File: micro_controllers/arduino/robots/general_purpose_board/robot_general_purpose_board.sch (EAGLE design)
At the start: 46 parts, among them IC1 ATMEGA328, IC2 7805, IC3 L293D, IC4 358, IC5 358, Q1 16MHZ

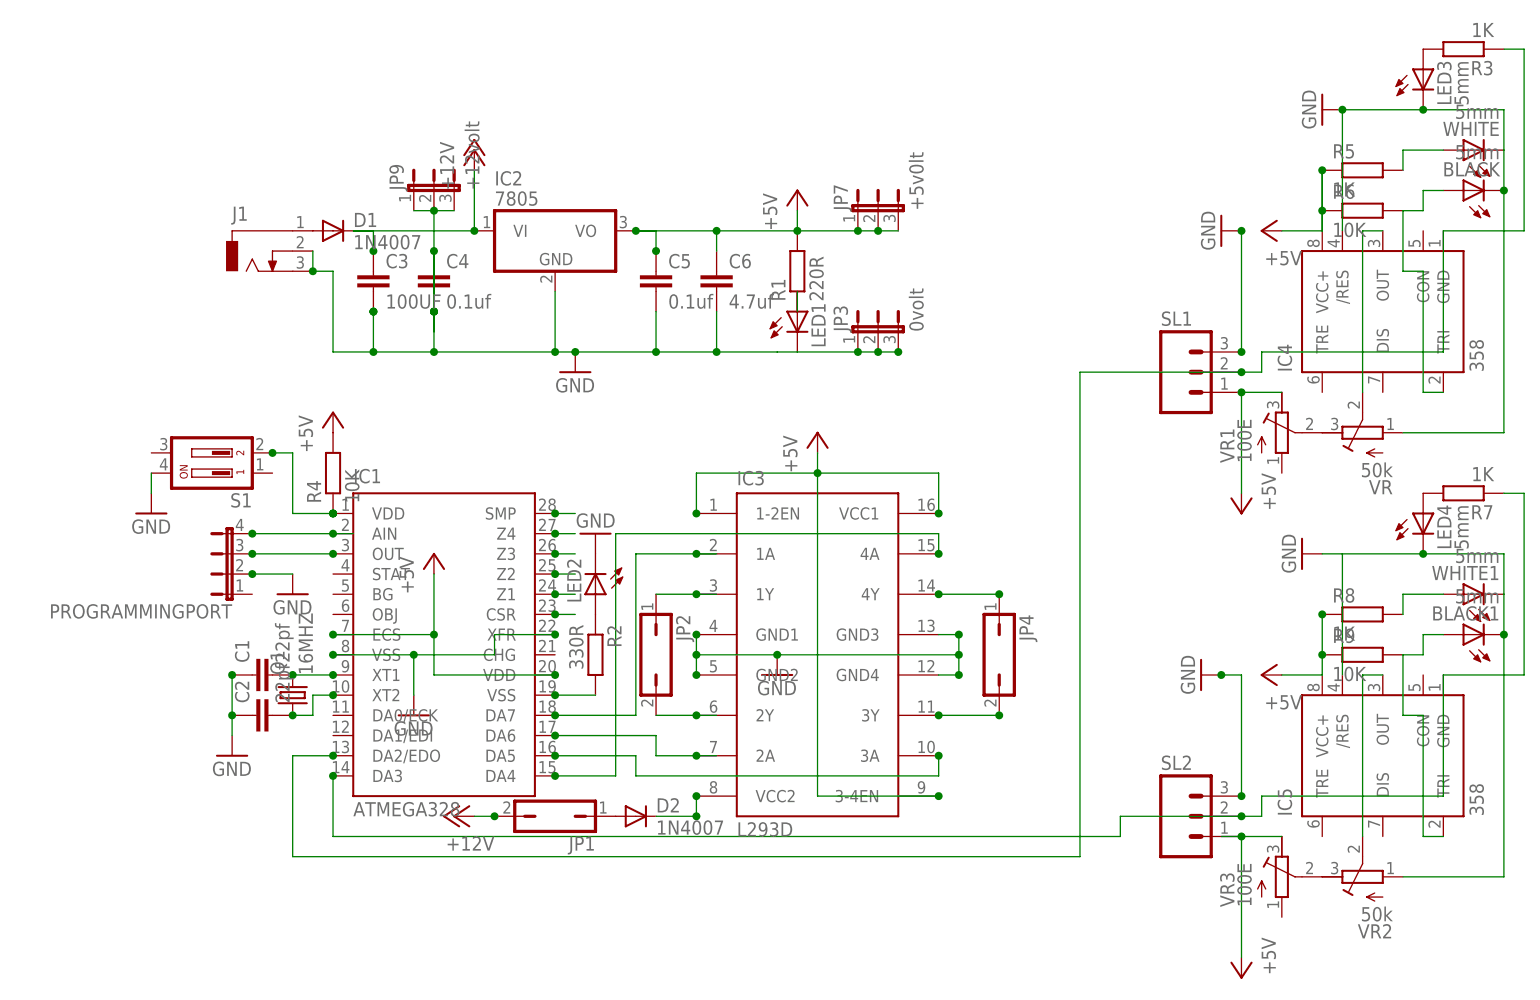
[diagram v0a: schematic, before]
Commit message: 
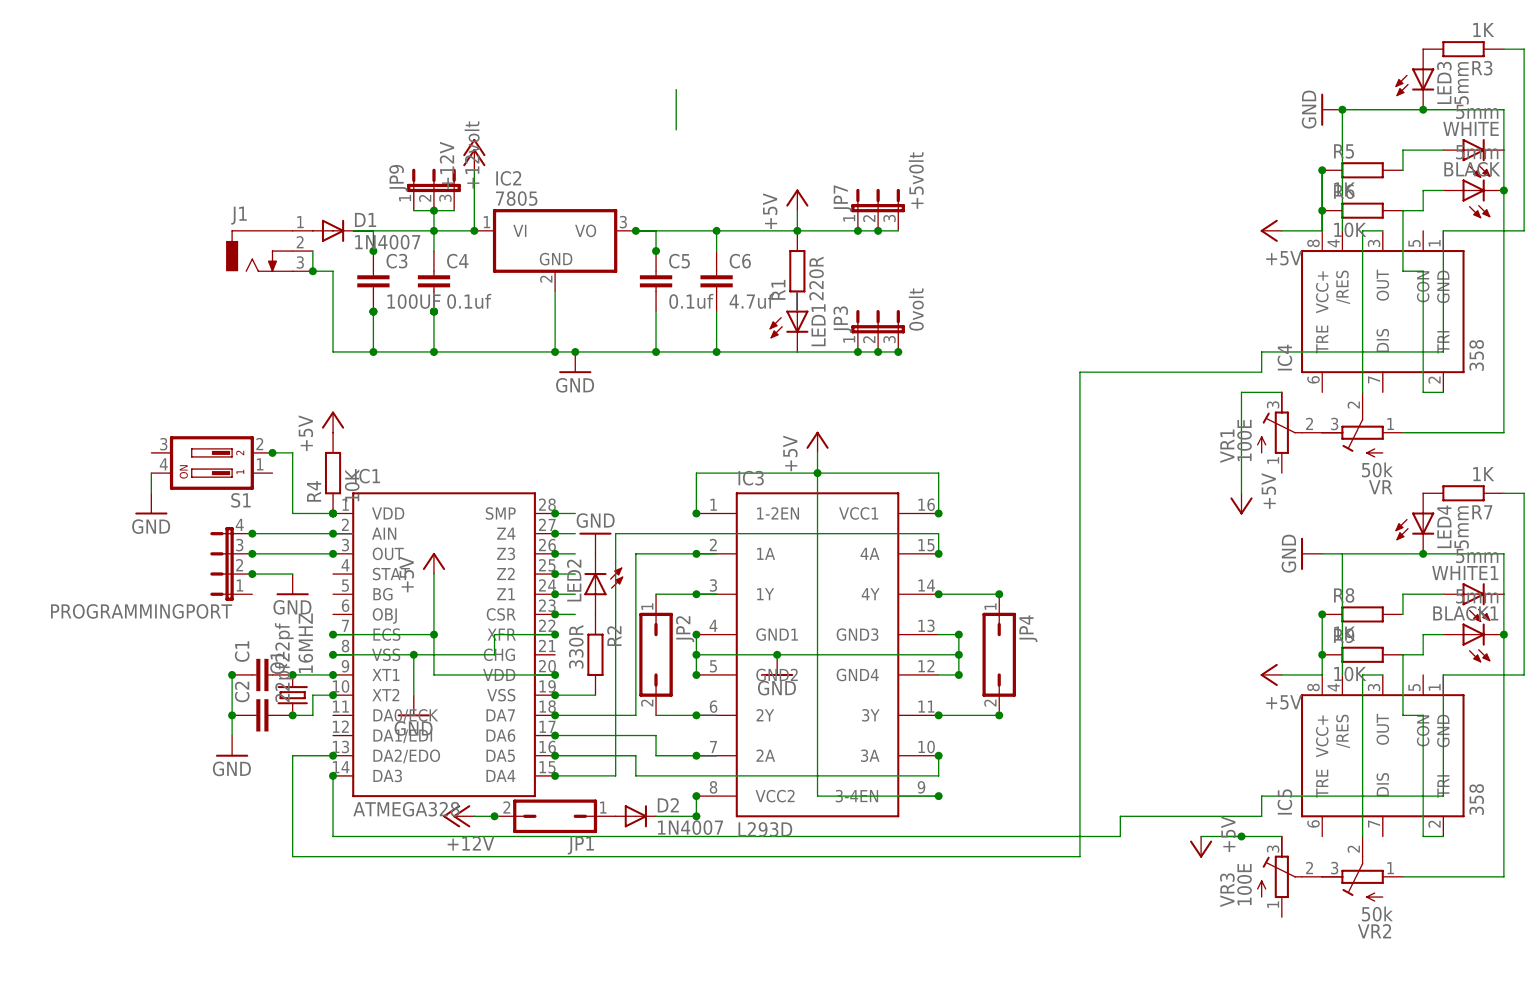
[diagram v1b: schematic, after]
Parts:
- removed SL1, SL2: (no value), con-amp-quick:M03
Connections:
- removed net N$4: C4.1
- net +12V: now also C4.1
- net +5V: no longer SL1.1, SL2.1
- net GND: no longer SL1.3, SL2.3
- net N$20: no longer SL1.2
- net N$34: no longer SL2.2
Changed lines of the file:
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@@
 <part name="VR" library="resistor" deviceset="R-TRIMM" device="64P" value="50k"/>
 <part name="WHITE" library="led" deviceset="LED" device="5MM" value="5mm"/>
-<part name="SL1" library="con-amp-quick" deviceset="M03" device=""/>
 <part name="BLACK" library="led" deviceset="LED" device="5MM" value="5mm"/>
 <part name="LED3" library="led" deviceset="LED" device="5MM" value="5mm"/>
@@
 <part name="VR2" library="resistor" deviceset="R-TRIMM" device="64P" value="50k"/>
 <part name="WHITE1" library="led" deviceset="LED" device="5MM" value="5mm"/>
-<part name="SL2" library="con-amp-quick" deviceset="M03" device=""/>
 <part name="BLACK1" library="led" deviceset="LED" device="5MM" value="5mm"/>
 <part name="LED4" library="led" deviceset="LED" device="5MM" value="5mm"/>
@@
 <part name="P+7" library="supply1" deviceset="+5V" device=""/>
 <part name="P+8" library="supply1" deviceset="+5V" device=""/>
-<part name="GND6" library="supply1" deviceset="GND" device=""/>
 <part name="GND8" library="supply1" deviceset="GND" device=""/>
 <part name="P+9" library="supply1" deviceset="+5V" device=""/>
 <part name="P+10" library="supply1" deviceset="+5V" device=""/>
 <part name="GND9" library="supply1" deviceset="GND" device=""/>
-<part name="GND10" library="supply1" deviceset="GND" device=""/>
 <part name="JP3" library="jumper" deviceset="JP2E" device="" value="0volt"/>
 <part name="GND11" library="supply1" deviceset="GND" device=""/>
@@
 <instance part="VR" gate="G$1" x="38.1" y="86.36" rot="R90"/>
 <instance part="WHITE" gate="G$1" x="50.8" y="121.92" rot="R90"/>
-<instance part="SL1" gate="G$1" x="15.24" y="93.98"/>
 <instance part="BLACK" gate="G$1" x="50.8" y="116.84" rot="R90"/>
 <instance part="LED3" gate="G$1" x="45.72" y="132.08"/>
@@
 <instance part="VR2" gate="G$1" x="38.1" y="30.48" rot="R90"/>
 <instance part="WHITE1" gate="G$1" x="50.8" y="66.04" rot="R90"/>
-<instance part="SL2" gate="G$1" x="15.24" y="38.1"/>
 <instance part="BLACK1" gate="G$1" x="50.8" y="60.96" rot="R90"/>
 <instance part="LED4" gate="G$1" x="45.72" y="76.2"/>
@@
 <instance part="P+7" gate="1" x="25.4" y="111.76" rot="R90"/>
 <instance part="P+8" gate="1" x="22.86" y="76.2" rot="R180"/>
-<instance part="GND6" gate="1" x="20.32" y="111.76" rot="R270"/>
 <instance part="GND8" gate="1" x="33.02" y="127" rot="R270"/>
 <instance part="P+9" gate="1" x="25.4" y="55.88" rot="R90"/>
-<instance part="P+10" gate="1" x="22.86" y="17.78" rot="R180"/>
+<instance part="P+10" gate="1" x="17.78" y="33.02" rot="R180"/>
 <instance part="GND9" gate="1" x="30.48" y="71.12" rot="R270"/>
-<instance part="GND10" gate="1" x="17.78" y="55.88" rot="R270"/>
 <instance part="JP3" gate="1" x="-22.86" y="99.06"/>
 <instance part="GND11" gate="1" x="-96.52" y="66.04"/>
@@
 </segment>
 <segment>
-<pinref part="SL1" gate="G$1" pin="1"/>
 <wire x1="27.94" y1="91.44" x2="22.86" y2="91.44" width="0.1524" layer="91"/>
 <pinref part="VR1" gate="G$1" pin="A"/>
 <pinref part="P+8" gate="1" pin="+5V"/>
 <wire x1="22.86" y1="78.74" x2="22.86" y2="91.44" width="0.1524" layer="91"/>
-<junction x="22.86" y="91.44"/>
 </segment>
 <segment>
@@
 <segment>
 <pinref part="P+10" gate="1" pin="+5V"/>
-<wire x1="22.86" y1="20.32" x2="22.86" y2="35.56" width="0.1524" layer="91"/>
+<wire x1="17.78" y1="35.56" x2="22.86" y2="35.56" width="0.1524" layer="91"/>
 <wire x1="22.86" y1="35.56" x2="20.32" y2="35.56" width="0.1524" layer="91"/>
-<pinref part="SL2" gate="G$1" pin="1"/>
 <junction x="22.86" y="35.56"/>
 <pinref part="VR3" gate="G$1" pin="A"/>
@@
 <pinref part="C6" gate="G$1" pin="2"/>
 <wire x1="-43.18" y1="101.6" x2="-43.18" y2="96.52" width="0.1524" layer="91"/>
-<wire x1="-43.18" y1="96.52" x2="-35.56" y2="96.52" width="0.1524" layer="91"/>
-<wire x1="-35.56" y1="96.52" x2="-33.02" y2="96.52" width="0.1524" layer="91"/>
+<wire x1="-43.18" y1="96.52" x2="-33.02" y2="96.52" width="0.1524" layer="91"/>
 <wire x1="-50.8" y1="96.52" x2="-43.18" y2="96.52" width="0.1524" layer="91"/>
 <junction x="-63.5" y="96.52"/>
@@
 </segment>
 <segment>
-<pinref part="SL1" gate="G$1" pin="3"/>
-<pinref part="GND6" gate="1" pin="GND"/>
-<wire x1="22.86" y1="96.52" x2="22.86" y2="111.76" width="0.1524" layer="91"/>
-<junction x="22.86" y="96.52"/>
-<junction x="22.86" y="111.76"/>
-</segment>
-<segment>
 <pinref part="WHITE1" gate="G$1" pin="C"/>
 <wire x1="55.88" y1="60.96" x2="55.88" y2="66.04" width="0.1524" layer="91"/>
@@
 </segment>
 <segment>
-<pinref part="SL2" gate="G$1" pin="3"/>
-<pinref part="GND10" gate="1" pin="GND"/>
-<wire x1="22.86" y1="40.64" x2="22.86" y2="55.88" width="0.1524" layer="91"/>
-<wire x1="22.86" y1="55.88" x2="20.32" y2="55.88" width="0.1524" layer="91"/>
-<junction x="22.86" y="40.64"/>
-<junction x="20.32" y="55.88"/>
-</segment>
-<segment>
 <pinref part="GND11" gate="1" pin="GND"/>
 <pinref part="PROGRAMMINGPORT" gate="G$1" pin="2"/>
 <wire x1="-96.52" y1="68.58" x2="-101.6" y2="68.58" width="0.1524" layer="91"/>
 <junction x="-101.6" y="68.58"/>
-</segment>
-</net>
-<net name="N$4" class="0">
-<segment>
-<pinref part="C4" gate="G$1" pin="1"/>
-<junction x="-78.74" y="109.22"/>
-<wire x1="-78.74" y1="109.22" x2="-78.74" y2="101.6" width="0.1524" layer="91"/>
 </segment>
 </net>
@@
 <wire x1="-88.9" y1="111.76" x2="-86.36" y2="111.76" width="0.1524" layer="91"/>
 <wire x1="-86.36" y1="111.76" x2="-86.36" y2="109.22" width="0.1524" layer="91"/>
-<wire x1="-78.74" y1="99.06" x2="-78.74" y2="111.76" width="0.1524" layer="91"/>
 <junction x="-86.36" y="109.22"/>
 <pinref part="D1" gate="1" pin="C"/>
@@
 <wire x1="-73.66" y1="119.38" x2="-73.66" y2="111.76" width="0.1524" layer="91"/>
 <junction x="-73.66" y="111.76"/>
+<pinref part="C4" gate="G$1" pin="1"/>
+<wire x1="-78.74" y1="111.76" x2="-78.74" y2="109.22" width="0.1524" layer="91"/>
+<junction x="-78.74" y="111.76"/>
 </segment>
 <segment>
@@
 <wire x1="48.26" y1="96.52" x2="25.4" y2="96.52" width="0.1524" layer="91"/>
 <wire x1="25.4" y1="96.52" x2="25.4" y2="93.98" width="0.1524" layer="91"/>
-<wire x1="25.4" y1="93.98" x2="22.86" y2="93.98" width="0.1524" layer="91"/>
-<pinref part="SL1" gate="G$1" pin="2"/>
-<junction x="22.86" y="93.98"/>
 <wire x1="48.26" y1="111.76" x2="58.42" y2="111.76" width="0.1524" layer="91"/>
 <wire x1="58.42" y1="111.76" x2="58.42" y2="134.62" width="0.1524" layer="91"/>
@@
 <wire x1="-96.52" y1="33.02" x2="2.54" y2="33.02" width="0.1524" layer="91"/>
 <wire x1="2.54" y1="33.02" x2="2.54" y2="93.98" width="0.1524" layer="91"/>
-<wire x1="2.54" y1="93.98" x2="22.86" y2="93.98" width="0.1524" layer="91"/>
+<wire x1="2.54" y1="93.98" x2="25.4" y2="93.98" width="0.1524" layer="91"/>
 <junction x="-91.44" y="45.72"/>
 </segment>
@@
 <wire x1="48.26" y1="40.64" x2="25.4" y2="40.64" width="0.1524" layer="91"/>
 <wire x1="25.4" y1="40.64" x2="25.4" y2="38.1" width="0.1524" layer="91"/>
-<wire x1="25.4" y1="38.1" x2="22.86" y2="38.1" width="0.1524" layer="91"/>
-<pinref part="SL2" gate="G$1" pin="2"/>
-<junction x="22.86" y="38.1"/>
 <wire x1="48.26" y1="55.88" x2="58.42" y2="55.88" width="0.1524" layer="91"/>
 <wire x1="58.42" y1="55.88" x2="58.42" y2="78.74" width="0.1524" layer="91"/>
@@
 <wire x1="-91.44" y1="35.56" x2="7.62" y2="35.56" width="0.1524" layer="91"/>
 <wire x1="7.62" y1="35.56" x2="7.62" y2="38.1" width="0.1524" layer="91"/>
-<wire x1="7.62" y1="38.1" x2="22.86" y2="38.1" width="0.1524" layer="91"/>
+<wire x1="7.62" y1="38.1" x2="25.4" y2="38.1" width="0.1524" layer="91"/>
 <junction x="-91.44" y="43.18"/>
 </segment>
@@
 </segment>
 </net>
+<net name="N$4" class="0">
+<segment>
+<wire x1="-48.26" y1="129.54" x2="-48.26" y2="124.46" width="0.1524" layer="91"/>
+</segment>
+</net>

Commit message: 
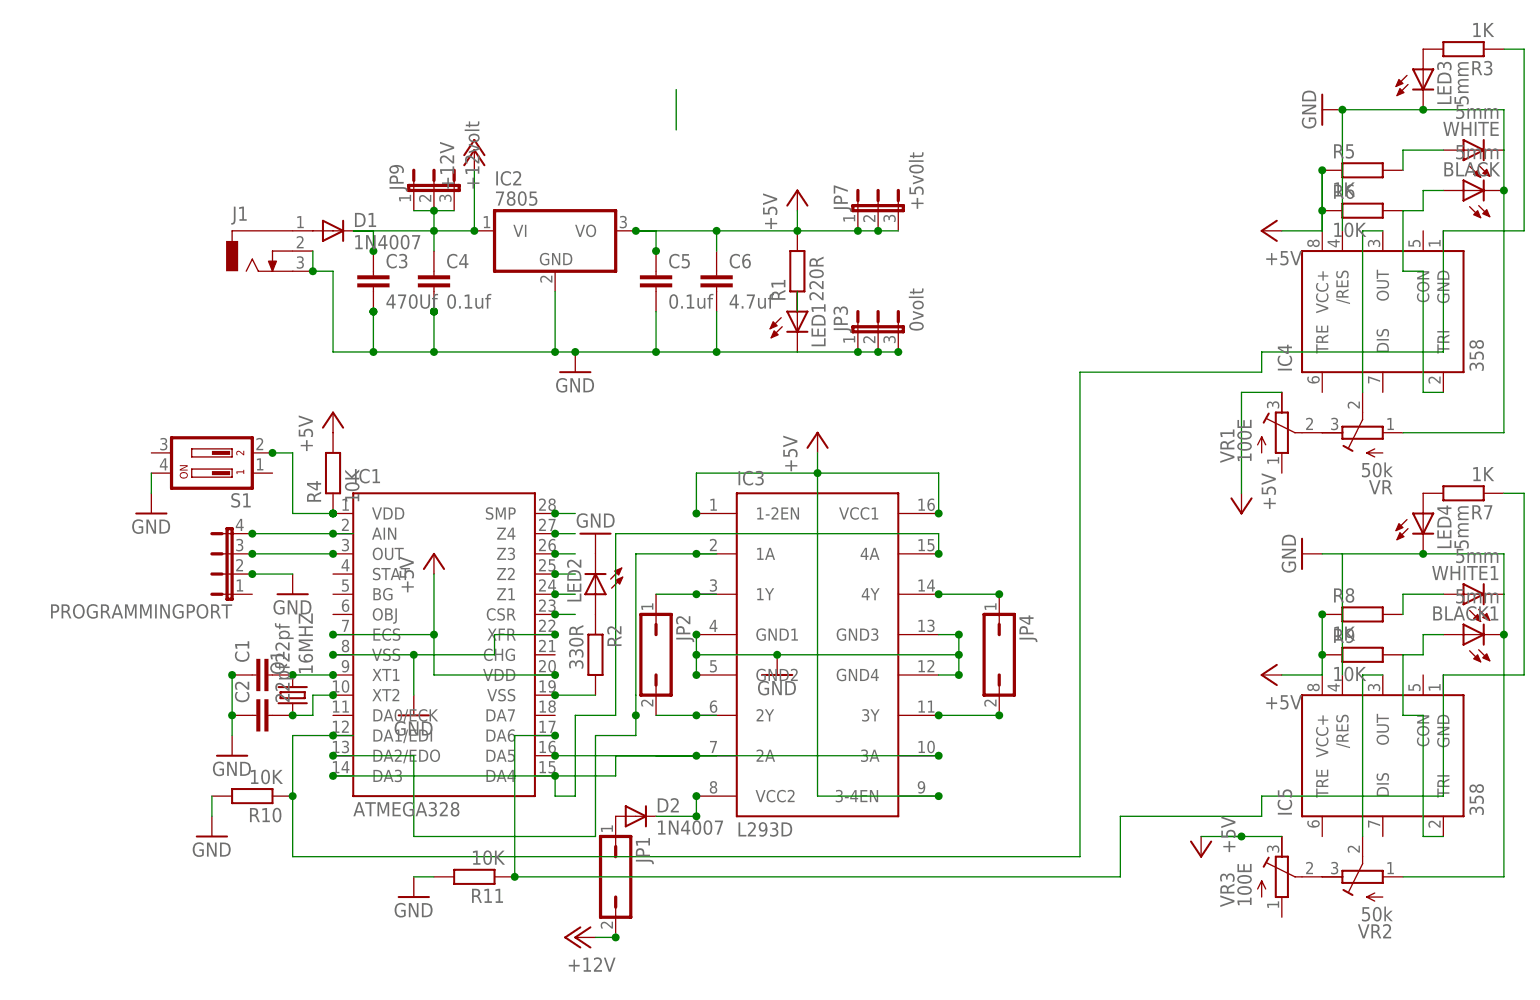
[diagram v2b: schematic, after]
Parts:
- added R10, R11: 10K, rcl:R-EU_0207/10
- C3: value 100UF -> 470Uf
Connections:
- removed net N$34: IC1.DA3, IC5.GND, R7.1
- new net N$33: IC1.DA2/EDO, IC3.1A
- net GND: now also R10.2, R11.2
- net N$20: now also IC1.DA1/EDI, R10.1; no longer IC1.DA2/EDO
- net N$25: now also IC1.DA3; no longer IC1.DA6
- net N$26: now also IC1.DA6, IC5.GND, R11.1, R7.1; no longer IC1.DA7, IC3.1A
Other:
- moved on the sheet: JP1
